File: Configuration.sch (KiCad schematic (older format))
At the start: 12 parts, among them CON1 AVR-JTAG-10, Q1 IRLML2502, Q2 IRLML2502, U1 xc7a50tftg256

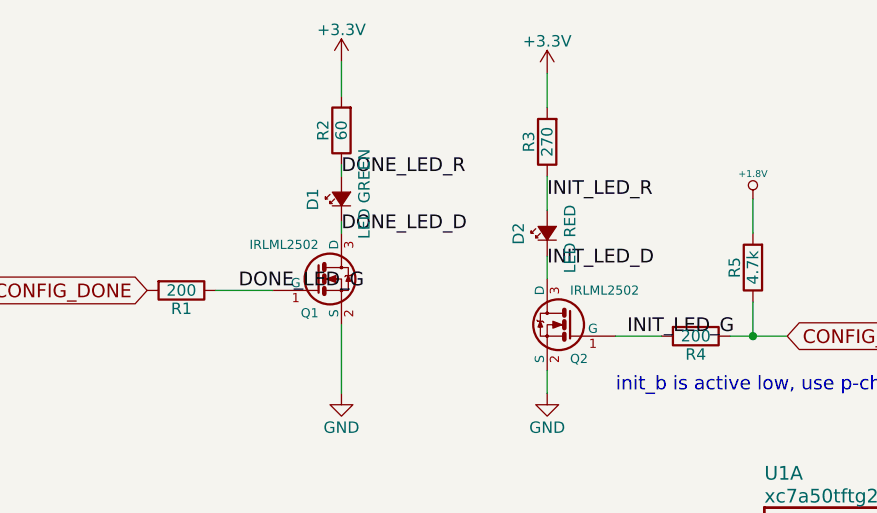
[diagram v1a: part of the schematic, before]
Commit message: completed BOM, changed footprints and values of identical components (ex. 100nf -> .1uF), have yet to update PCBNEW to reflect footprint changes
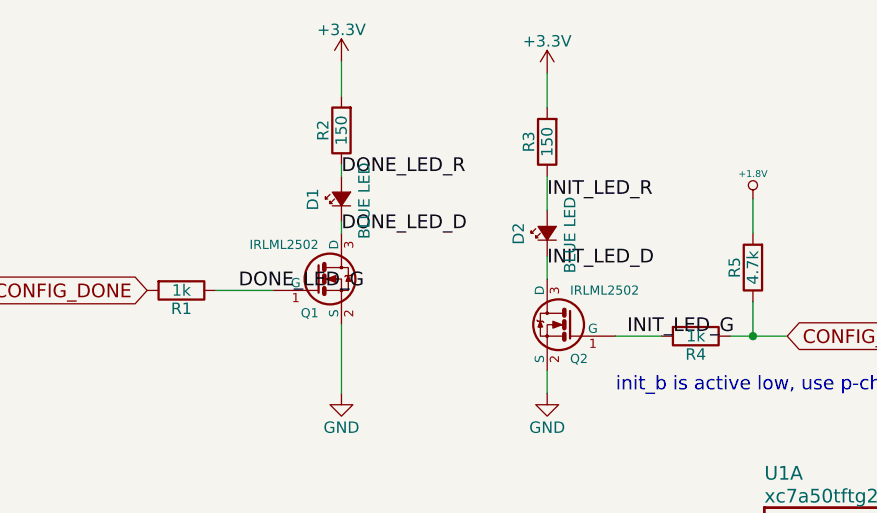
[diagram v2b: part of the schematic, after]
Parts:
- D1: value LED GREEN -> BLUE LED
- D2: value LED RED -> BLUE LED
- R1, R4: value 200 -> 1k
- R2: value 60 -> 150
- R3: value 270 -> 150
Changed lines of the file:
@@
 P 4550 1450
 F 0 "D2" H 4500 1575 50  0000 L CNN
-F 1 "LED RED" H 4375 1350 50  0000 L CNN
+F 1 "BLUE LED" H 4375 1350 50  0000 L CNN
 F 2 "LEDs:LED_0603" V 4550 1450 50  0001 C CNN
 F 3 "" V 4550 1450 50  0000 C CNN
@@
 P 3650 1300
 F 0 "D1" H 3600 1425 50  0000 L CNN
-F 1 "LED GREEN" H 3475 1200 50  0000 L CNN
+F 1 "BLUE LED" H 3475 1200 50  0000 L CNN
 F 2 "LEDs:LED_0603" V 3650 1300 50  0001 C CNN
 F 3 "" V 3650 1300 50  0000 C CNN
@@
 P 3650 1000
 F 0 "R2" V 3730 1000 50  0000 C CNN
-F 1 "60" V 3650 1000 50  0000 C CNN
+F 1 "150" V 3650 1000 50  0000 C CNN
 F 2 "Resistors_SMD:R_0402" V 3580 1000 50  0001 C CNN
 F 3 "" H 3650 1000 50  0000 C CNN
@@
 P 4550 1050
 F 0 "R3" V 4630 1050 50  0000 C CNN
-F 1 "270" V 4550 1050 50  0000 C CNN
+F 1 "150" V 4550 1050 50  0000 C CNN
 F 2 "Resistors_SMD:R_0402" V 4480 1050 50  0001 C CNN
 F 3 "" H 4550 1050 50  0000 C CNN
@@
 P 2950 1700
 F 0 "R1" V 3030 1700 50  0000 C CNN
-F 1 "200" V 2950 1700 50  0000 C CNN
+F 1 "1k" V 2950 1700 50  0000 C CNN
 F 2 "Resistors_SMD:R_0402" V 2880 1700 50  0001 C CNN
 F 3 "" H 2950 1700 50  0000 C CNN
@@
 P 5200 1900
 F 0 "R4" V 5280 1900 50  0000 C CNN
-F 1 "200" V 5200 1900 50  0000 C CNN
+F 1 "1k" V 5200 1900 50  0000 C CNN
 F 2 "Resistors_SMD:R_0402" V 5130 1900 50  0001 C CNN
 F 3 "" H 5200 1900 50  0000 C CNN

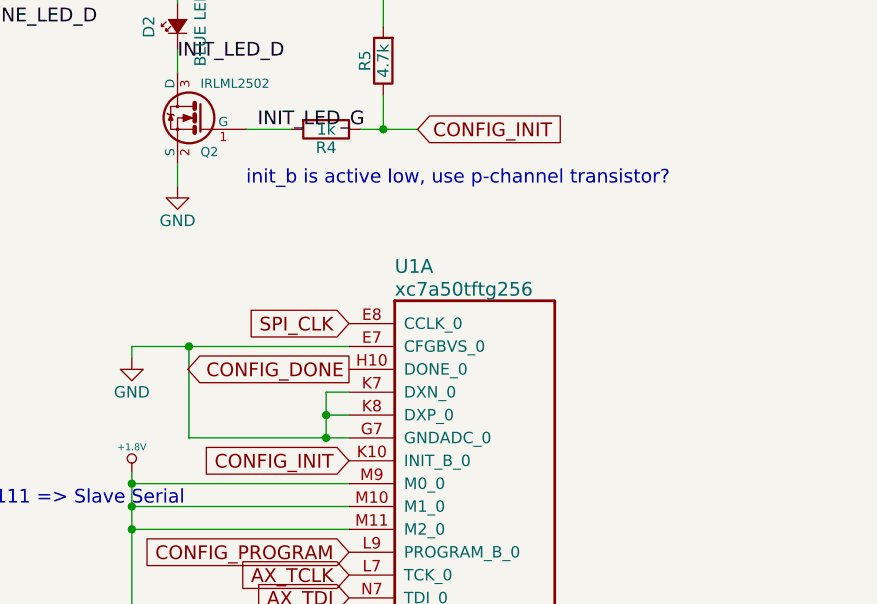
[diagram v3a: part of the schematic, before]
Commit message: added configuration data line, other small changes
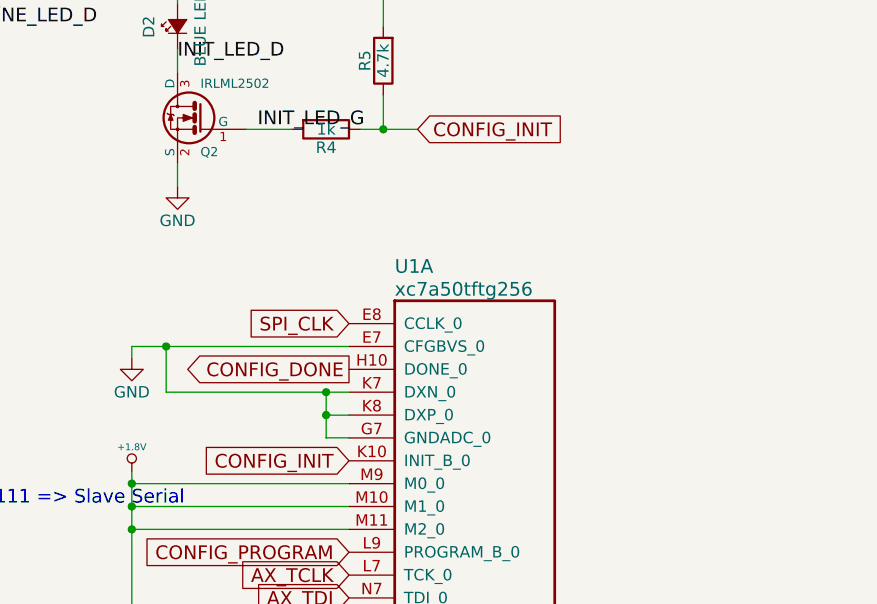
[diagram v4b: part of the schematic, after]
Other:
- note removed: "init_b is active low, use p-channel transistor?"
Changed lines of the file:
@@
 CONFIG_DONE
 $Comp
-L +1.8V #PWR6
+L +1.8V #PWR01
 U 1 1 585C3A3C
 P 4350 3400
-F 0 "#PWR6" H 4350 3540 20  0001 C CNN
+F 0 "#PWR01" H 4350 3540 20  0001 C CNN
 F 1 "+1.8V" H 4350 3510 30  0000 C CNN
 F 2 "" H 4350 3400 60  0001 C CNN
@@
 $EndComp
 $Comp
-L GND #PWR10
+L GND #PWR02
 U 1 1 585C2834
 P 5050 4950
-F 0 "#PWR10" H 5050 4700 50  0001 C CNN
+F 0 "#PWR02" H 5050 4700 50  0001 C CNN
 F 1 "GND" H 5050 4800 50  0000 C CNN
 F 2 "" H 5050 4950 50  0000 C CNN
@@
 	4350 3400 4350 4300
 Wire Wire Line
-	5300 3150 5200 3150
-Wire Wire Line
-	5200 3050 5200 3250
-Connection ~ 5200 3250
-Wire Wire Line
-	5300 3050 5200 3050
-Connection ~ 5200 3150
+	4500 3050 5300 3050
 Wire Wire Line
 	4350 2850 5300 2850
-Wire Wire Line
-	4600 2850 4600 3250
 Wire Wire Line
 	5300 4450 5200 4450
@@
 NoConn ~ 2250 4100
 $Comp
-L GND #PWR1
+L GND #PWR03
 U 1 1 585C40A7
 P 1550 4400
-F 0 "#PWR1" H 1550 4150 50  0001 C CNN
+F 0 "#PWR03" H 1550 4150 50  0001 C CNN
 F 1 "GND" H 1550 4250 50  0000 C CNN
 F 2 "" H 1550 4400 50  0000 C CNN
@@
 $EndComp
 $Comp
-L +1.8V #PWR2
+L +1.8V #PWR04
 U 1 1 585C40DD
 P 1650 3650
-F 0 "#PWR2" H 1650 3790 20  0001 C CNN
+F 0 "#PWR04" H 1650 3790 20  0001 C CNN
 F 1 "+1.8V" H 1650 3760 30  0000 C CNN
 F 2 "" H 1650 3650 60  0001 C CNN
@@
 	4350 4500 4350 4550
 $Comp
-L GND #PWR7
+L GND #PWR05
 U 1 1 586C7770
 P 4350 4550
-F 0 "#PWR7" H 4350 4300 50  0001 C CNN
+F 0 "#PWR05" H 4350 4300 50  0001 C CNN
 F 1 "GND" H 4350 4400 50  0000 C CNN
 F 2 "" H 4350 4550 50  0000 C CNN
@@
 	3650 700  3650 850
 $Comp
-L GND #PWR4
+L GND #PWR06
 U 1 1 5875AB8B
 P 3650 2150
-F 0 "#PWR4" H 3650 1900 50  0001 C CNN
+F 0 "#PWR06" H 3650 1900 50  0001 C CNN
 F 1 "GND" H 3650 2000 50  0000 C CNN
 F 2 "" H 3650 2150 50  0000 C CNN
@@
 	4550 1200 4550 1350
 $Comp
-L +3.3V #PWR3
+L +3.3V #PWR07
 U 1 1 5876ED3D
 P 3650 700
-F 0 "#PWR3" H 3650 550 50  0001 C CNN
+F 0 "#PWR07" H 3650 550 50  0001 C CNN
 F 1 "+3.3V" H 3650 840 50  0000 C CNN
 F 2 "" H 3650 700 50  0000 C CNN
@@
 Connection ~ 5450 1900
 $Comp
-L +1.8V #PWR11
+L +1.8V #PWR08
 U 1 1 587E84F9
 P 5450 1300
-F 0 "#PWR11" H 5450 1440 20  0001 C CNN
+F 0 "#PWR08" H 5450 1440 20  0001 C CNN
 F 1 "+1.8V" H 5450 1410 30  0000 C CNN
 F 2 "" H 5450 1300 60  0001 C CNN
@@
 Connection ~ 4350 3650
 $Comp
-L GND #PWR5
+L GND #PWR09
 U 1 1 587E913C
 P 4350 2900
-F 0 "#PWR5" H 4350 2650 50  0001 C CNN
+F 0 "#PWR09" H 4350 2650 50  0001 C CNN
 F 1 "GND" H 4350 2750 50  0000 C CNN
 F 2 "" H 4350 2900 50  0000 C CNN
@@
 Wire Wire Line
 	4350 2850 4350 2900
-Connection ~ 4600 2850
-Wire Wire Line
-	4600 3250 5300 3250
 Wire Wire Line
 	5050 4850 5300 4850
@@
 	4550 750  4550 900
 $Comp
-L +3.3V #PWR8
+L +3.3V #PWR010
 U 1 1 587E9CAF
 P 4550 750
-F 0 "#PWR8" H 4550 600 50  0001 C CNN
+F 0 "#PWR010" H 4550 600 50  0001 C CNN
 F 1 "+3.3V" H 4550 890 50  0000 C CNN
 F 2 "" H 4550 750 50  0000 C CNN
@@
 $EndComp
 $Comp
-L GND #PWR9
+L GND #PWR011
 U 1 1 587E9EC7
 P 4550 2150
-F 0 "#PWR9" H 4550 1900 50  0001 C CNN
+F 0 "#PWR011" H 4550 1900 50  0001 C CNN
 F 1 "GND" H 4550 2000 50  0000 C CNN
 F 2 "" H 4550 2150 50  0000 C CNN
@@
 Text Label 3650 1450 0    60   ~ 0
 DONE_LED_D
-Text Notes 4850 2150 0    60   ~ 0
-init_b is active low, use p-channel transistor?
+Wire Wire Line
+	5300 3150 5200 3150
+Wire Wire Line
+	5200 3050 5200 3250
+Wire Wire Line
+	4500 2850 4500 3050
+Connection ~ 5200 3050
+Connection ~ 4500 2850
+Wire Wire Line
+	5200 3250 5300 3250
+Connection ~ 5200 3150
 $EndSCHEMATC

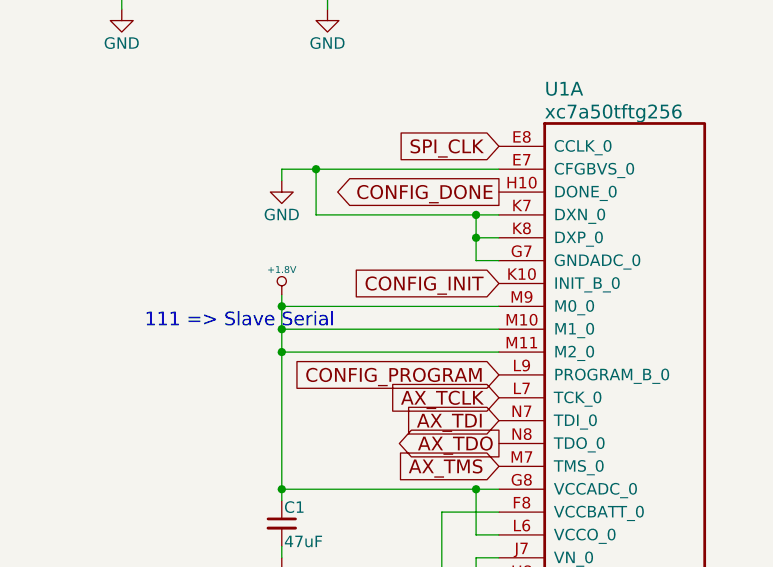
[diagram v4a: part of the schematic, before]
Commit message: thickened USB sig traces, centered footprints, and other small changes
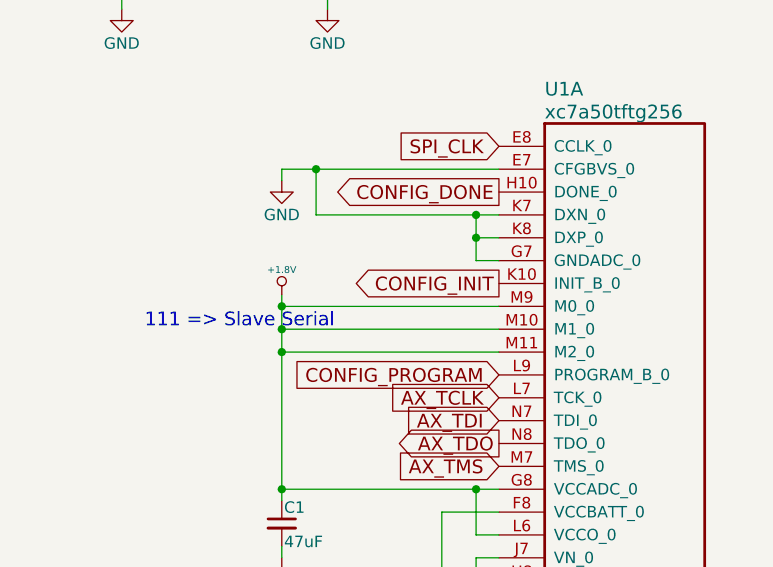
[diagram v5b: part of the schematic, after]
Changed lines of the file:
@@
 	-1   0    0    1
 $EndComp
-Text GLabel 5300 3350 0    60   Input ~ 0
+Text GLabel 5300 3350 0    60   Output ~ 0
 CONFIG_INIT
 Wire Wire Line

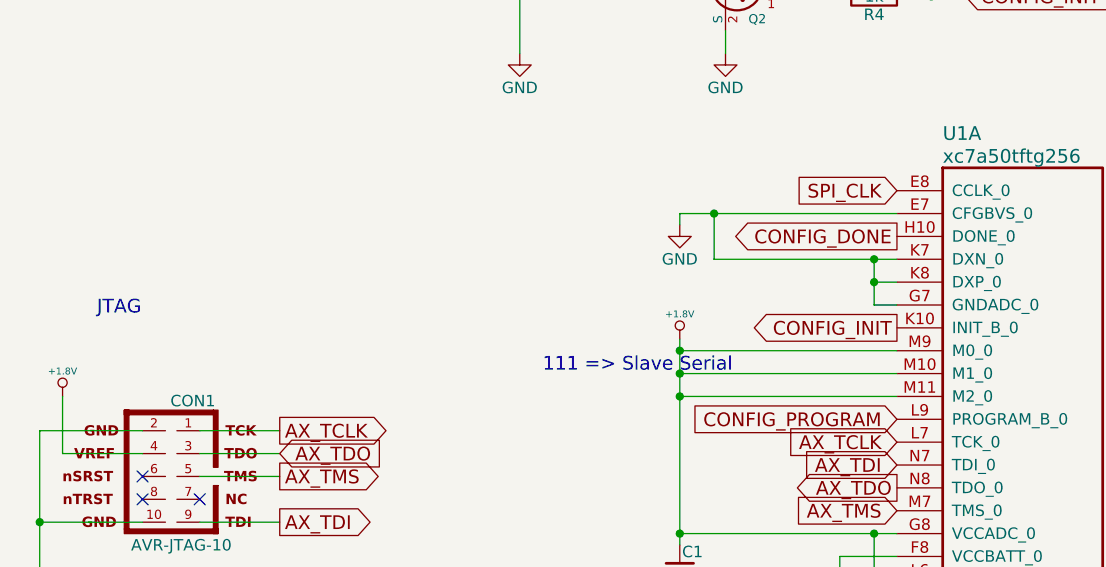
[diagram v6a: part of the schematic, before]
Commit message: forced insert on J7, HDMI connector
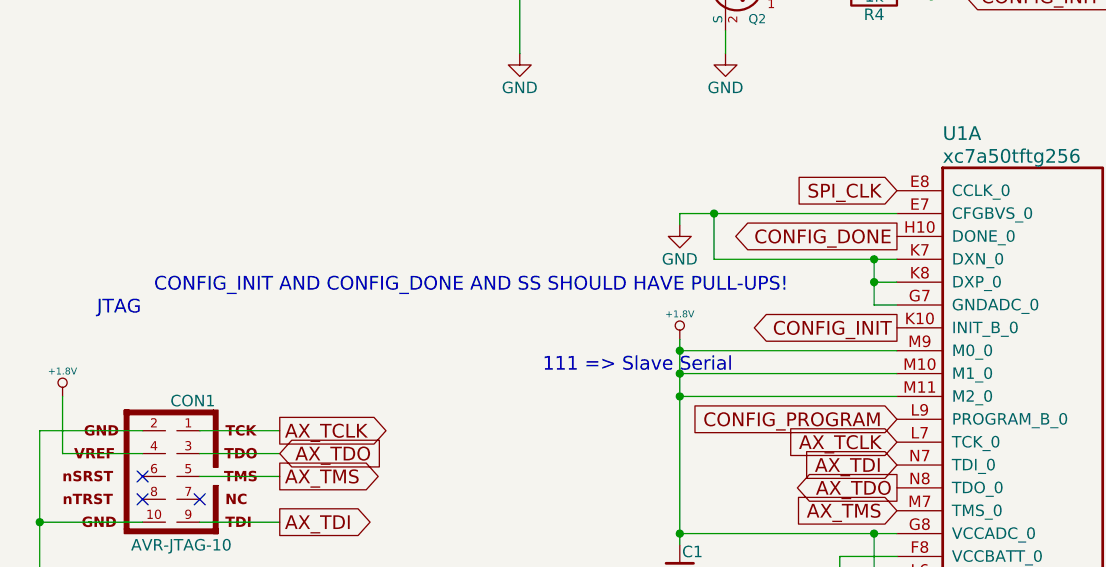
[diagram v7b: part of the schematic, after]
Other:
- note added: "CONFIG_INIT AND CONFIG_DONE AND SS SHOULD HAVE PULL-UPS!"
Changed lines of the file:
@@
 	5200 3250 5300 3250
 Connection ~ 5200 3150
+Text Notes 2050 3200 0    60   ~ 0
+CONFIG_INIT AND CONFIG_DONE AND SS SHOULD HAVE PULL-UPS!
 $EndSCHEMATC

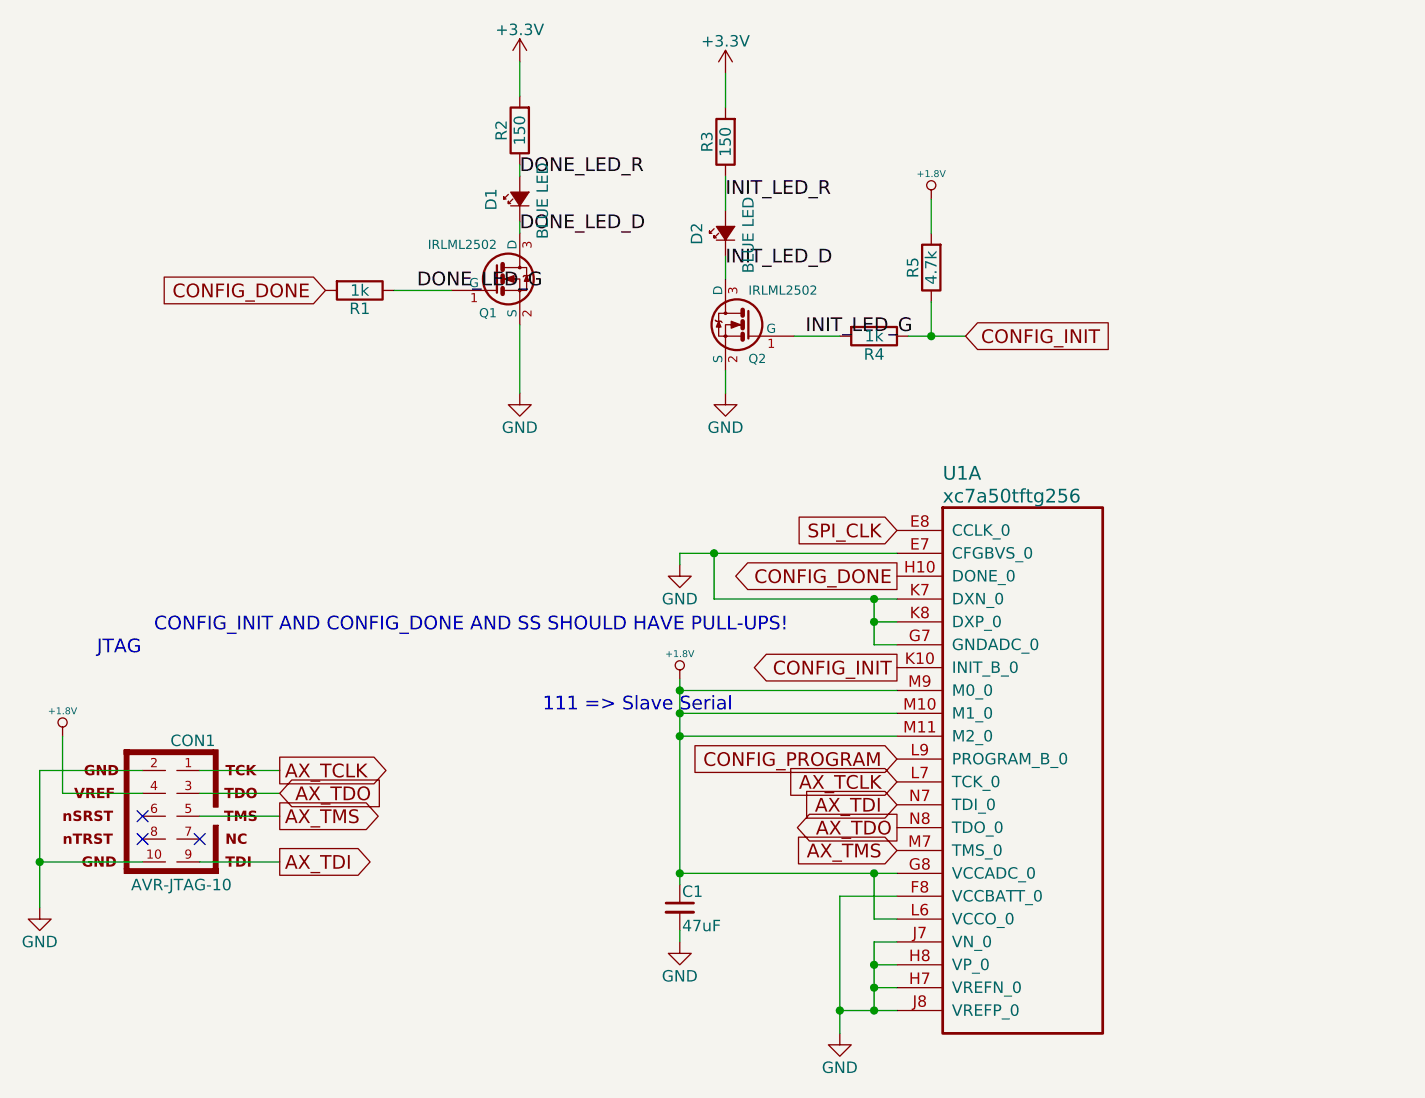
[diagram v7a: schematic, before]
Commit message: relocation of components for second prototype run, replacement of LCD with 50-pin ZIF connector for ILI9341
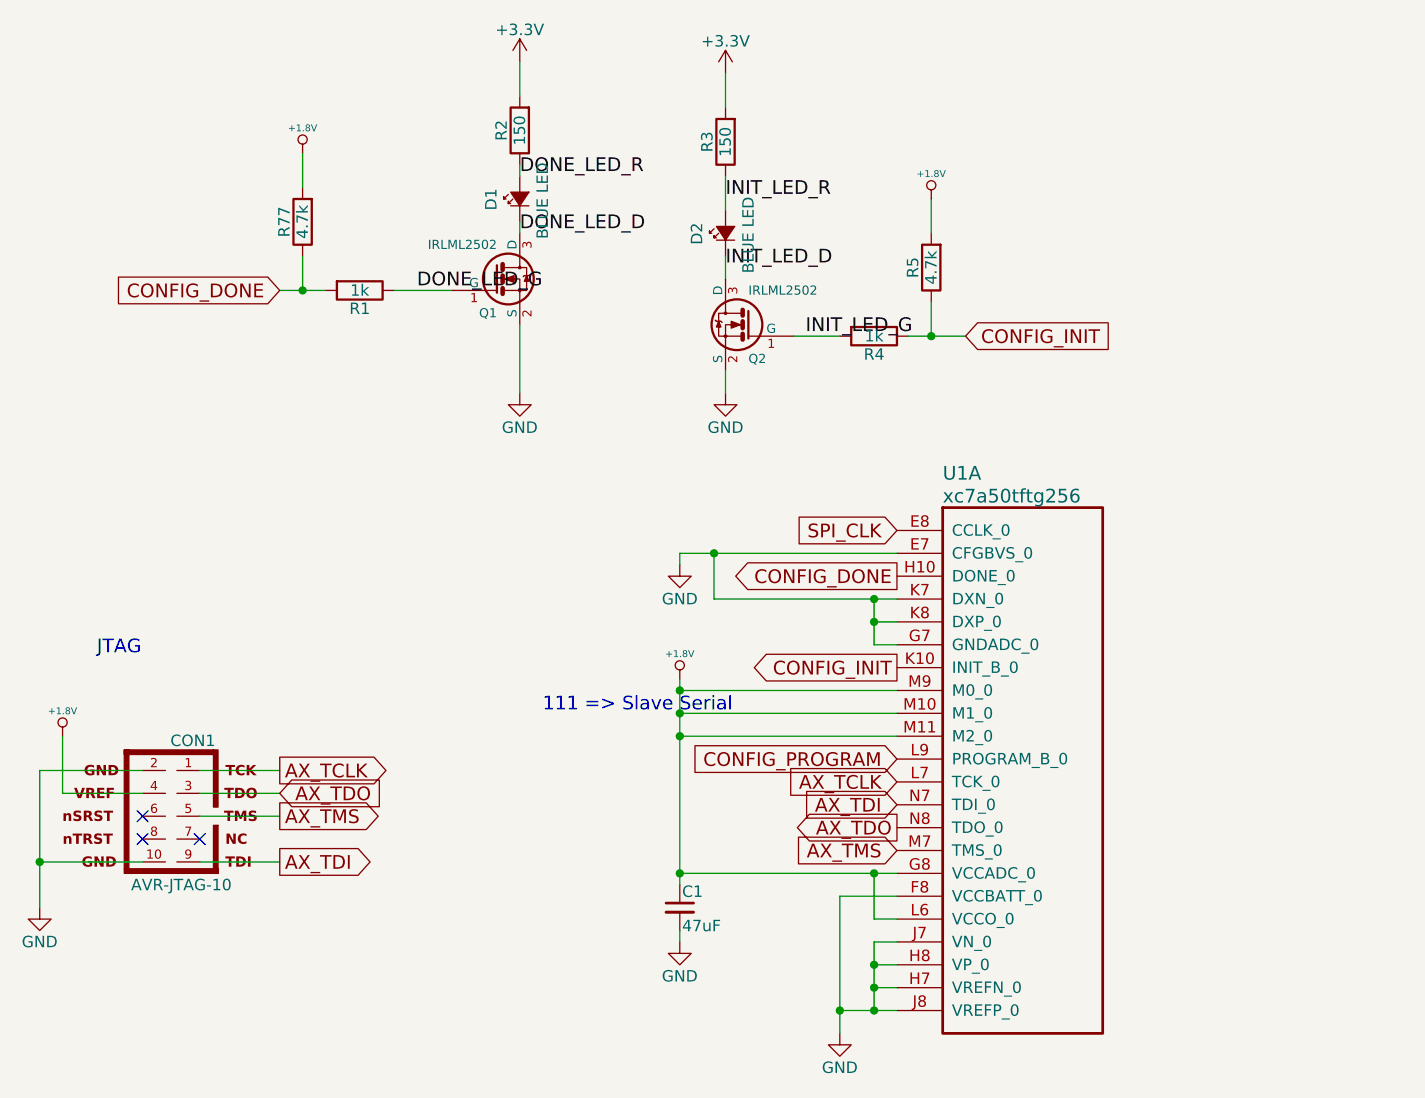
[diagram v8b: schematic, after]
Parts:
- added R77: 4.7k, Resistors_SMD:R_0402, symbol R
- CON1: footprint DFTcustom:CustomJTAG -> DFTcustom:XilinxJTAG
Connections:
- net +1.8V: now also R77.2
- net CONFIG_DONE: now also R77.1
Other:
- note removed: "CONFIG_INIT AND CONFIG_DONE AND SS SHOULD HAVE PULL-UPS!"
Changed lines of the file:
@@
 LIBS:N25Q128A
 LIBS:sparkfun
-LIBS:GSB3211311WEU
 LIBS:48258-0001
 LIBS:ArduinoSpecAn-cache
@@
 LIBS:tps22963c
 LIBS:gndtie
+LIBS:GSB3211311WEU
+LIBS:DFTCustom
 EELAYER 25 0
 EELAYER END
 $Descr A4 11693 8268
 encoding utf-8
-Sheet 3 16
+Sheet 3 15
 Title ""
 Date ""
@@
 F 0 "CON1" H 1880 4330 50  0000 C CNN
 F 1 "AVR-JTAG-10" H 1710 3670 50  0000 L BNN
-F 2 "DFTcustom:CustomJTAG" V 1480 4020 50  0001 C CNN
+F 2 "DFTcustom:XilinxJTAG" V 1480 4020 50  0001 C CNN
 F 3 "" H 2050 4000 50  0000 C CNN
 	1    2050 4000
@@
 Wire Wire Line
 	2600 4000 2250 4000
-Text GLabel 2800 1700 0    60   Input ~ 0
+Text GLabel 2600 1700 0    60   Input ~ 0
 CONFIG_DONE
 Text GLabel 5600 1900 2    60   Input ~ 0
@@
 	5200 3250 5300 3250
 Connection ~ 5200 3150
-Text Notes 2050 3200 0    60   ~ 0
-CONFIG_INIT AND CONFIG_DONE AND SS SHOULD HAVE PULL-UPS!
+$Comp
+L R R77
+U 1 1 5908E731
+P 2700 1400
+F 0 "R77" V 2780 1400 50  0000 C CNN
+F 1 "4.7k" V 2700 1400 50  0000 C CNN
+F 2 "Resistors_SMD:R_0402" V 2630 1400 50  0001 C CNN
+F 3 "" H 2700 1400 50  0000 C CNN
+	1    2700 1400
+	-1   0    0    1
+$EndComp
+Wire Wire Line
+	2700 1550 2700 1700
+$Comp
+L +1.8V #PWR012
+U 1 1 5908E738
+P 2700 1100
+F 0 "#PWR012" H 2700 1240 20  0001 C CNN
+F 1 "+1.8V" H 2700 1210 30  0000 C CNN
+F 2 "" H 2700 1100 60  0001 C CNN
+F 3 "" H 2700 1100 60  0001 C CNN
+	1    2700 1100
+	1    0    0    -1
+$EndComp
+Wire Wire Line
+	2700 1100 2700 1250
+Wire Wire Line
+	2600 1700 2800 1700
+Connection ~ 2700 1700
 $EndSCHEMATC
